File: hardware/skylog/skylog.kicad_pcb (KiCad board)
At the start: 2 copper layers, 5 parts, among them U1 ESP32-DevKitC, U2 Sensor_TempUmid_RS485_5V_24V, U3 KY-028, U4 GY-302_BH1750, U5 RS485_TTL_V2_OSHWLab

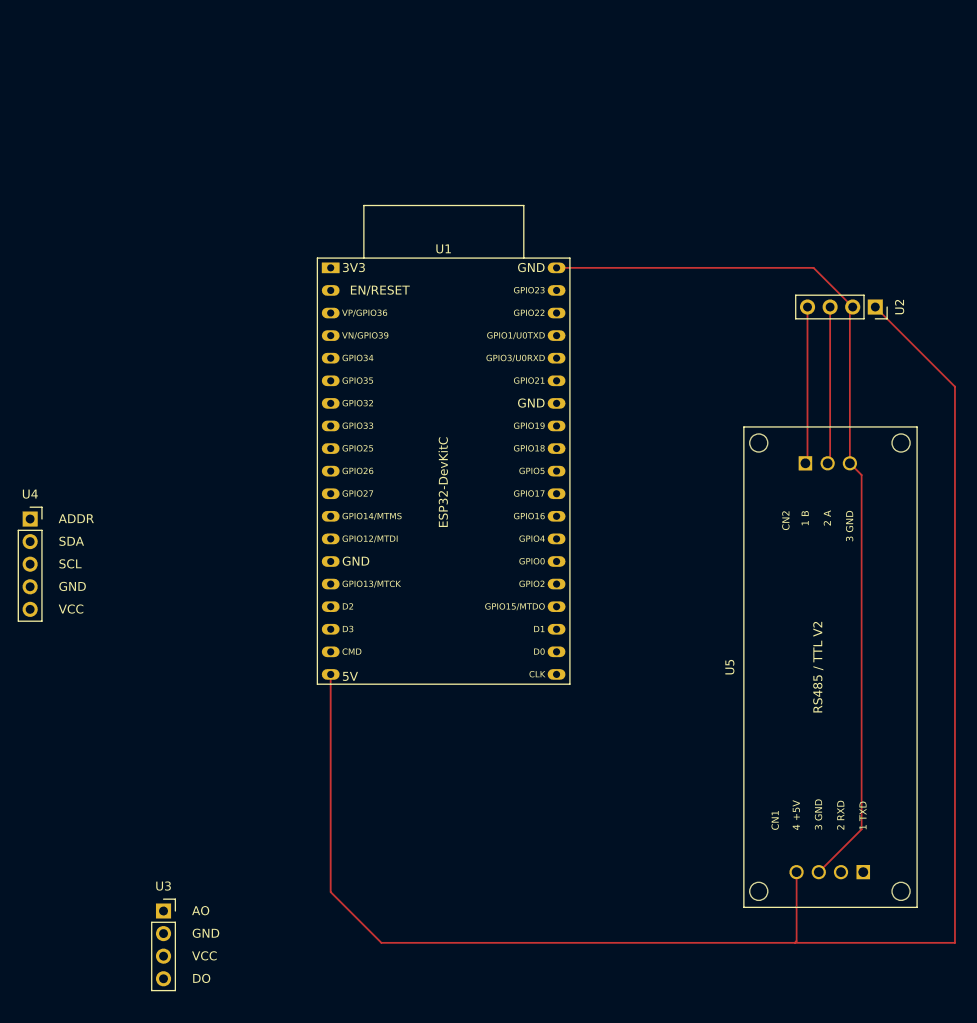
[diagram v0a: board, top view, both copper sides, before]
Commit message: Refactor KiCad project files by removing unused libraries and updating footprints
- Removed references to unused libraries "Sensores_Modulos" and "ESP32" from fp-lib-table and sym-lib-table.
- Updated footprint references in the schematic for ESP32 from "ESP32:ESP32-DevKitC" to "PCM_Espressif:ESP32-DevKitC".
- Adjusted footprint positions and properties for KY-028 and GY-302 components in the PCB layout, including rotation and alignment changes.
- Modified net connections and segment paths in the PCB layout for improved routing and clarity.
- Cleaned up designators in the project file, removing unused designators for better organization.
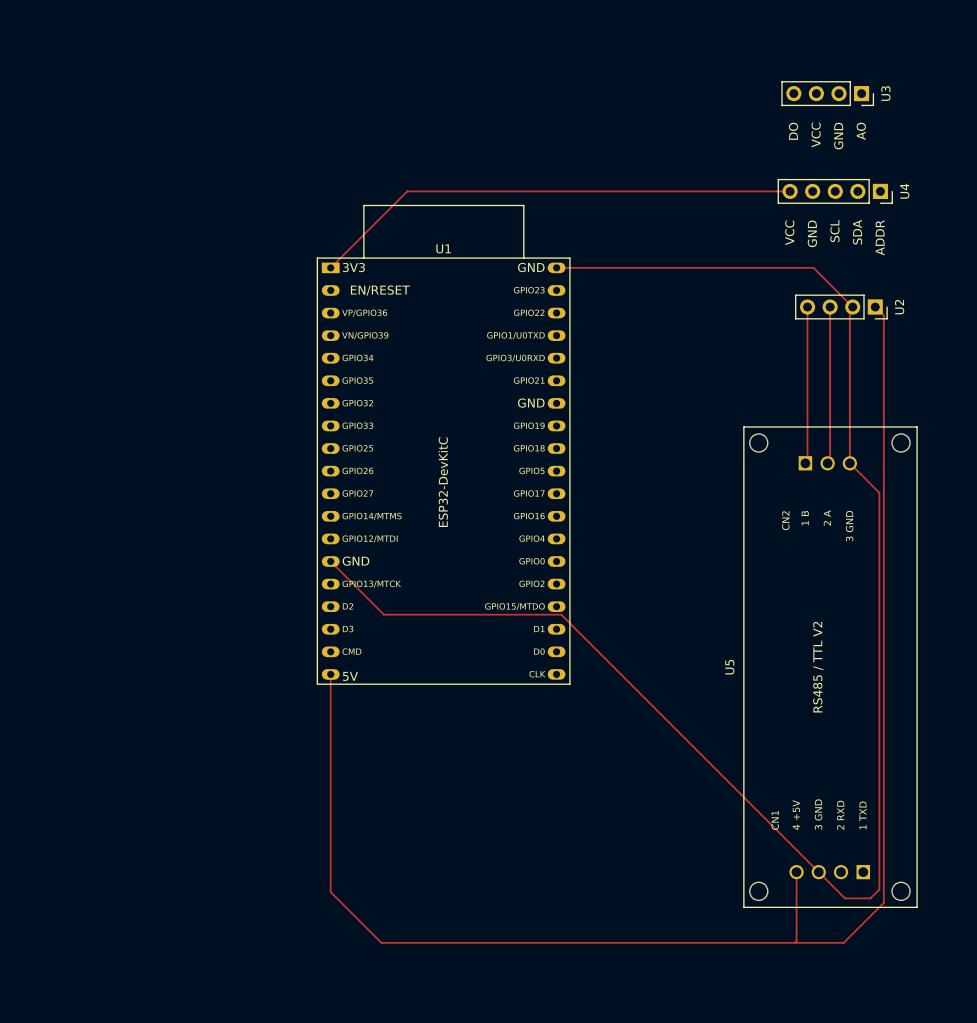
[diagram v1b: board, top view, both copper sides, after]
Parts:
- moved U3 120.9 mm to (233.0, 25.5), turned to -90 degrees
- moved U4 102.5 mm to (235.1, 36.5), turned to -90 degrees
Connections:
- U1 pad 3: Net-(U1-SENSOR_VN/GPIO39/ADC1_CH3) -> unconnected-(U1-SENSOR_VP/GPIO36/ADC1_CH0-Pad3)
- U1 pad 4: Net-(U1-SENSOR_VN/GPIO39/ADC1_CH3) -> unconnected-(U1-SENSOR_VN/GPIO39/ADC1_CH3-Pad4)
- U1 pad 6: Net-(U1-SENSOR_VN/GPIO39/ADC1_CH3) -> Net-(U1-VDET_2/GPIO35/ADC1_CH7)
- U3 pad 1: Net-(U1-SENSOR_VN/GPIO39/ADC1_CH3) -> Net-(U1-VDET_2/GPIO35/ADC1_CH7)
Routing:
- net /GND_SENSOR: track 101.3 -> 179.9 mm
- net Net-(U1-3V3): track 0.00 -> 55.2 mm
- net /VIN_SENSOR: track 180.3 -> 166.3 mm

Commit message: Add new footprints for wire jumpers and pads; update symbol library table
- Created a new footprint for a 10mm wire jumper (Wire_Jumper_P10.00mm) with specifications for soldered connections and pad dimensions.
- Added a footprint for a wire pad (Wire_Pad_D1.2mm) designed for insulated power wire connections, including pad and drill sizes.
- Updated the symbol library table to include additional libraries for Espressif components, sensor modules, and standard power symbols for KiCad 10.
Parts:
- added J1: ENS160+AHT21, skylog:ENS160_AHT21_1x04_P2.54mm, F.Cu at (207.0, 25.5)
- added J2: WEMOS_5V, skylog:Wire_Pad_D1.2mm, F.Cu at (168.0, 94.0)
- added J3: WEMOS_GND, skylog:Wire_Pad_D1.2mm, F.Cu at (162.0, 94.0)
- U1: footprint ESP32:ESP32-DevKitC -> skylog:ESP32-DevKitC_BoardEdge
- moved U1 26.1 mm to (173.3, 19.0)
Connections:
- U1 pad 27: unconnected-(U1-GPIO16-Pad27) -> /RS485_RX
- U1 pad 28: unconnected-(U1-GPIO17-Pad28) -> /RS485_TX
- U1 pad 34: Net-(U1-U0RXD/GPIO3) -> unconnected-(U1-U0RXD/GPIO3-Pad34)
- U1 pad 35: Net-(U1-U0TXD/GPIO1) -> unconnected-(U1-U0TXD/GPIO1-Pad35)
- U4 pad 1: unconnected-(U4-ADDR-Pad1) -> /GND_SENSOR
- U5 pad CN1.1: Net-(U1-U0TXD/GPIO1) -> /RS485_TX
- U5 pad CN1.2: Net-(U1-U0RXD/GPIO3) -> /RS485_RX
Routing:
- net /GND_SENSOR: track 179.9 -> 0.00 mm
- net Net-(U1-GPIO21): track 0.00 -> 99.6 mm
- net /RS485_TX: track 0.00 -> 83.1 mm
- net /RS485_RX: track 0.00 -> 79.5 mm
- net Net-(U1-GPIO22): track 0.00 -> 72.8 mm
- net Net-(U1-VDET_2/GPIO35/ADC1_CH7): track 0.00 -> 62.6 mm
- net Net-(U1-3V3): track 55.2 -> 71.4 mm
- net /VIN_SENSOR: track 166.3 -> 170.0 mm
- added copper zone on B.Cu, net /GND_SENSOR
- added copper zone on F.Cu, net /GND_SENSOR
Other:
- board outline added: 86 x 111 mm
- board text added: "5V"
- board text added: "GND"
